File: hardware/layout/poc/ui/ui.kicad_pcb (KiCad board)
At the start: 2 copper layers, 49.5 x 40.5 mm, 18 parts, among them J1 JST-SH 1x10, J2 OLED, SW1 PRG/RST, SW2 FUNC, U1 74AHCT1G125

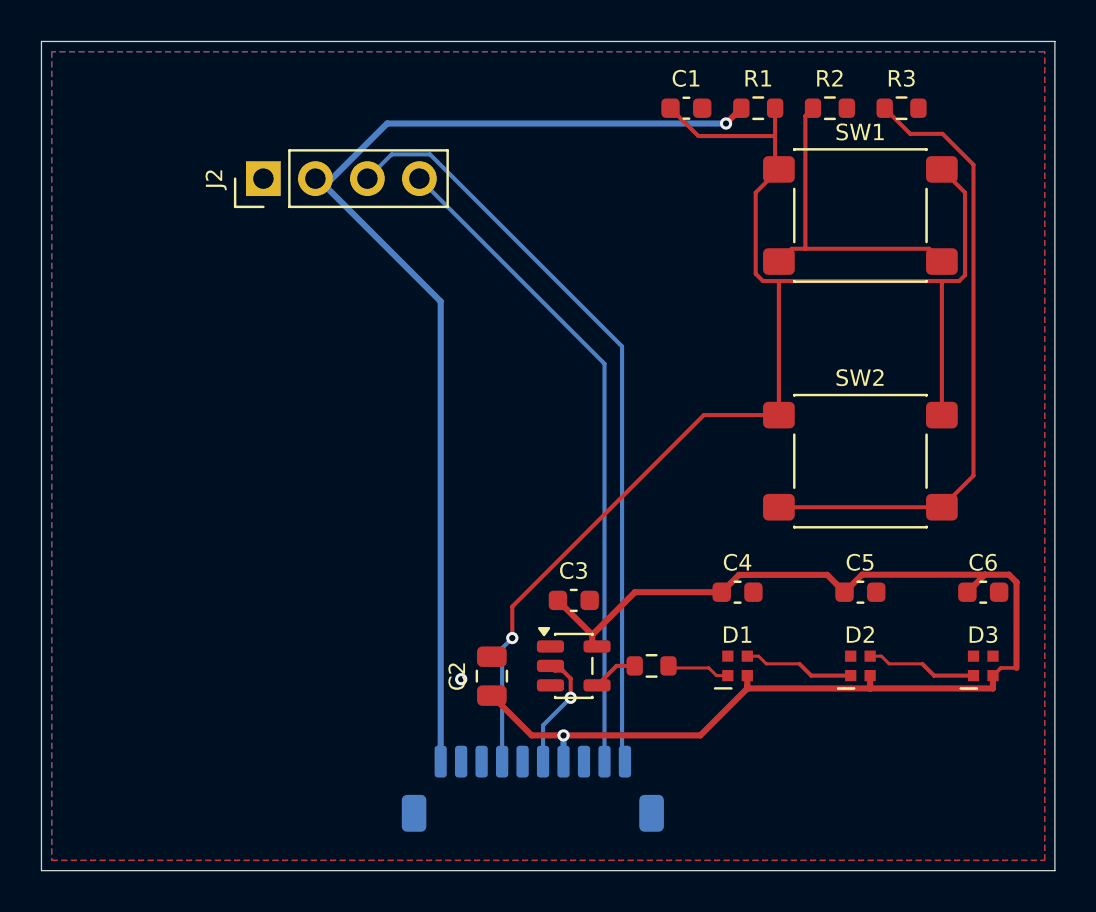
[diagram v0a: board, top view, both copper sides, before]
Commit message: CI matrix for hardware variants (poc/v2); updated AGENTS.md with V2 details and verification workflow
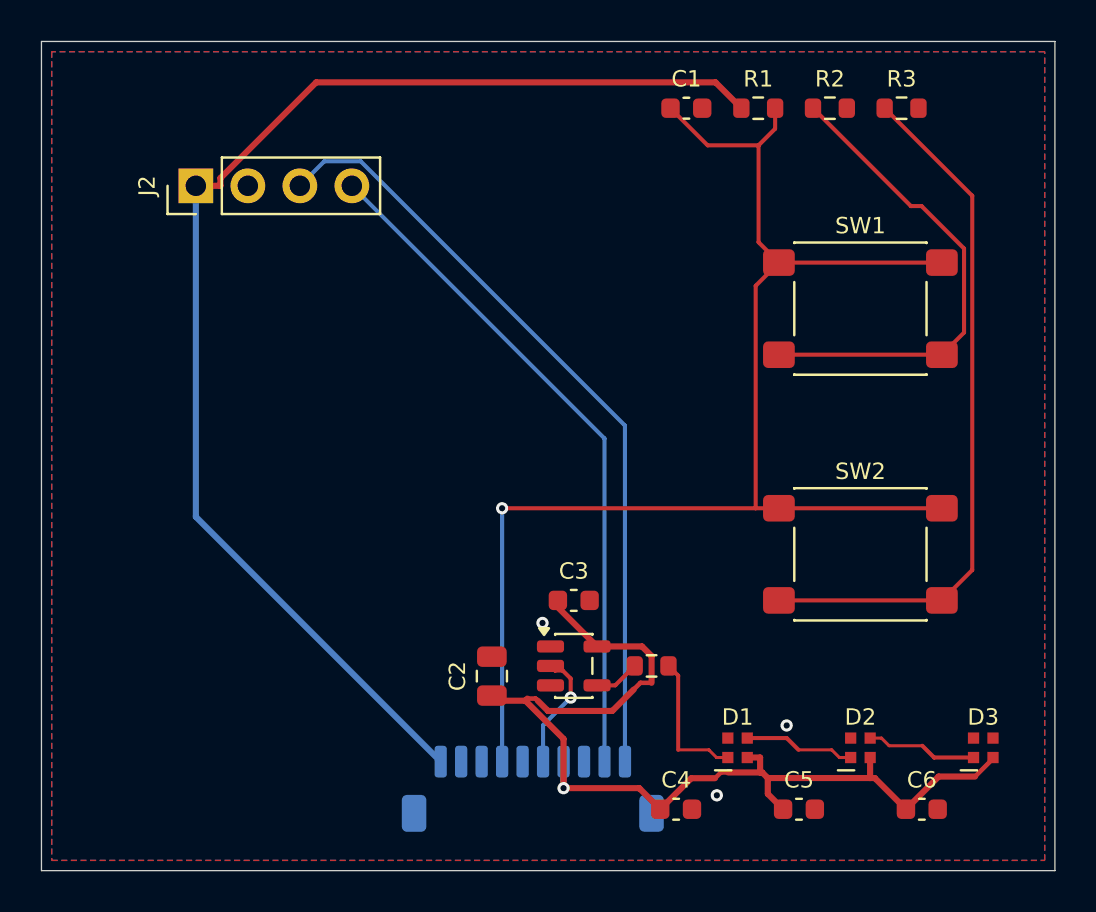
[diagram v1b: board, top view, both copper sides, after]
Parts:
- moved C4 11.0 mm to (31.0, -3.00)
- moved C5 11.0 mm to (37.0, -3.00)
- moved C6 11.0 mm to (43.0, -3.00)
- moved SW1 4.55 mm to (40.0, -27.4)
- moved SW2 4.55 mm to (40.0, -15.4)
- moved D1 4.00 mm to (34.0, -6.00)
- moved D2 4.00 mm to (40.0, -6.00)
- moved D3 4.00 mm to (46.0, -6.00)
- moved J2 3.32 mm to (7.54, -33.5)
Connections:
- D1 pad 1: LED_CHAIN1 -> N$4
- D1 pad 2: GND -> +5V
- D1 pad 3: N$4 -> LED_CHAIN1
- D1 pad 4: +5V -> GND
- D2 pad 1: LED_CHAIN2 -> LED_CHAIN1
- D2 pad 2: GND -> +5V
- D2 pad 3: LED_CHAIN1 -> LED_CHAIN2
- D2 pad 4: +5V -> GND
- D3 pad 1: (no net) -> LED_CHAIN2
- D3 pad 2: GND -> +5V
- D3 pad 3: LED_CHAIN2 -> (no net)
- D3 pad 4: +5V -> GND
- J2 pad 1: GND -> +3V3
- J2 pad 2: +3V3 -> GND
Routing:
- net +5V: track 61.9 -> 50.5 mm
- net +3V3: track 53.0 -> 62.6 mm, vias 1 -> 0
- net N$1: track 15.5 -> 23.8 mm
- net N$4: track 3.16 -> 6.88 mm
- net N$2: track 30.8 -> 34.4 mm
- net I2C_SDA: track 32.2 -> 33.2 mm
- net I2C_SCL: track 37.2 -> 38.1 mm
- net BTN_LADDER: track 68.2 -> 67.6 mm
- net GND: vias 1 -> 3
